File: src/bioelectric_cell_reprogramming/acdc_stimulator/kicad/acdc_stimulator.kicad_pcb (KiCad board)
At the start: 4 copper layers, 139 x 133 mm, 144 parts, among them IC1 AD9833BRM-REEL7, IC2 AD5122BCPZ10-RL7, IC3 LTC3896EFE#PBF, IC4 LTC3637IMSE#PBF, IC5 LTC3637IMSE#PBF, IC6 LTC3637IMSE#PBF, J1 Screw_Terminal_01x02, J2 Conn_ARM_SWD_TagConnect_TC203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, J3 USB_C_Receptacle_USB2.0_14P, J4 S4B-PH-SM4-TB, J5 IPL1-102-01-L-S-K, J6 Screw_Terminal_01x02, J7 IPL1-102-01-L-S-K, J8 6620XX11122_66200211122, J9 6620XX11122_66200211122, Q1 BSZ096N10LS5ATMA1, Q10 BSZ096N10LS5ATMA1, Q11 BSZ096N10LS5ATMA1, Q2 NDT3055L, Q3 BSC520N15NS3G, Q4 BSC520N15NS3G, Q5 IPD320N20N3GATMA1, Q6 BSZ096N10LS5ATMA1, Q7 BSZ096N10LS5ATMA1, Q8 IPB320P10LMATMA1, Q9 IPB320P10LMATMA1, SW1 SW_Push, SW2 SW_SPDT, U1 STM32G473RCTx, U2 AMS1117-3.3, U3 USBLC6-2SC6, U4 LTC6090CFE-PBF, U5 LTC6090CFE-PBF, U7 DRV8873HPWPR, Y1 16Mhz

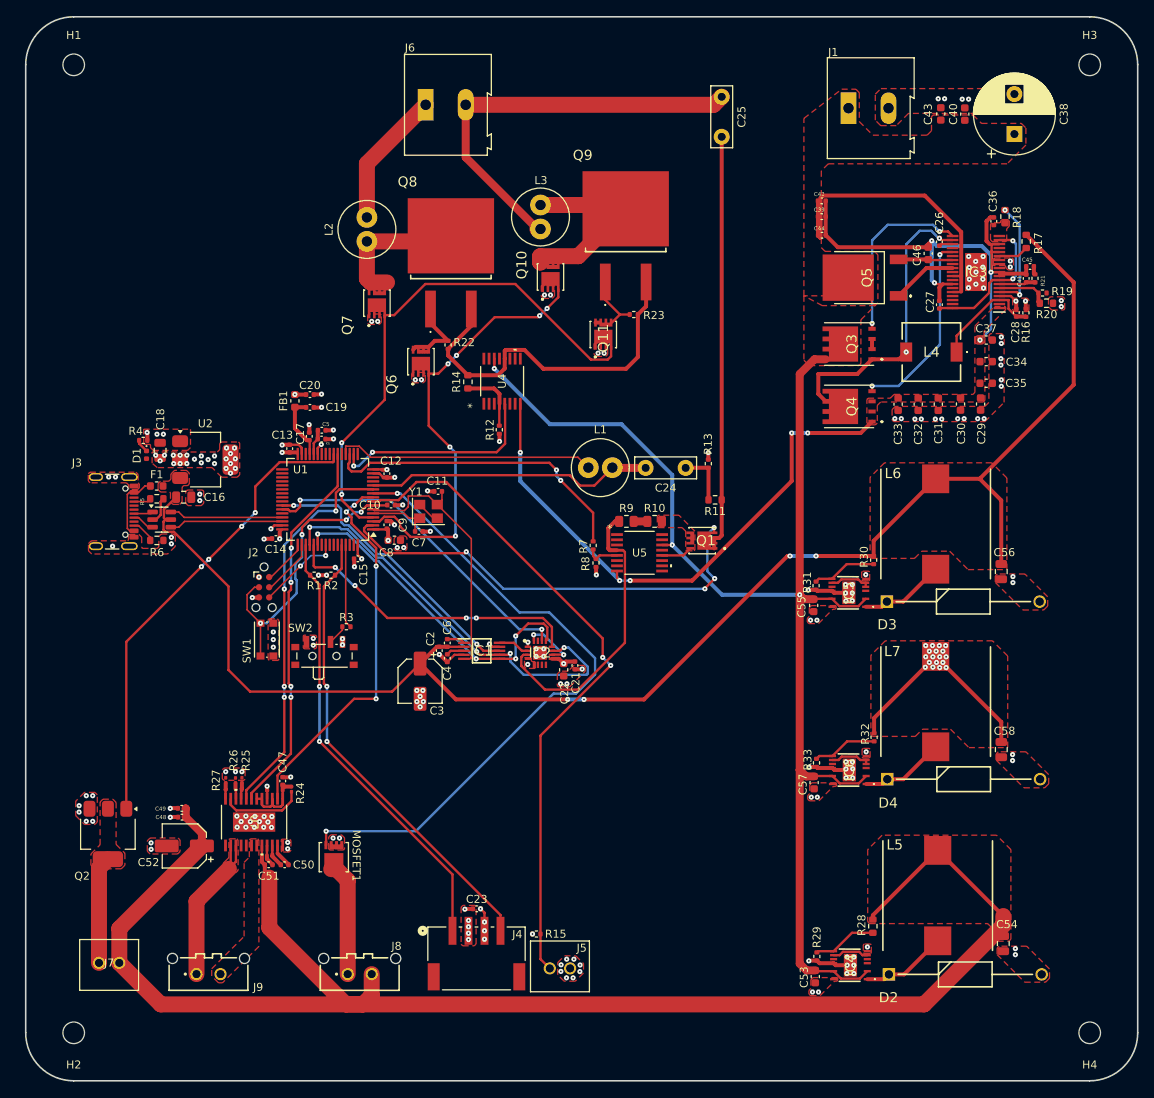
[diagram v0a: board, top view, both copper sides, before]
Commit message: fix: cleared all DRC errors
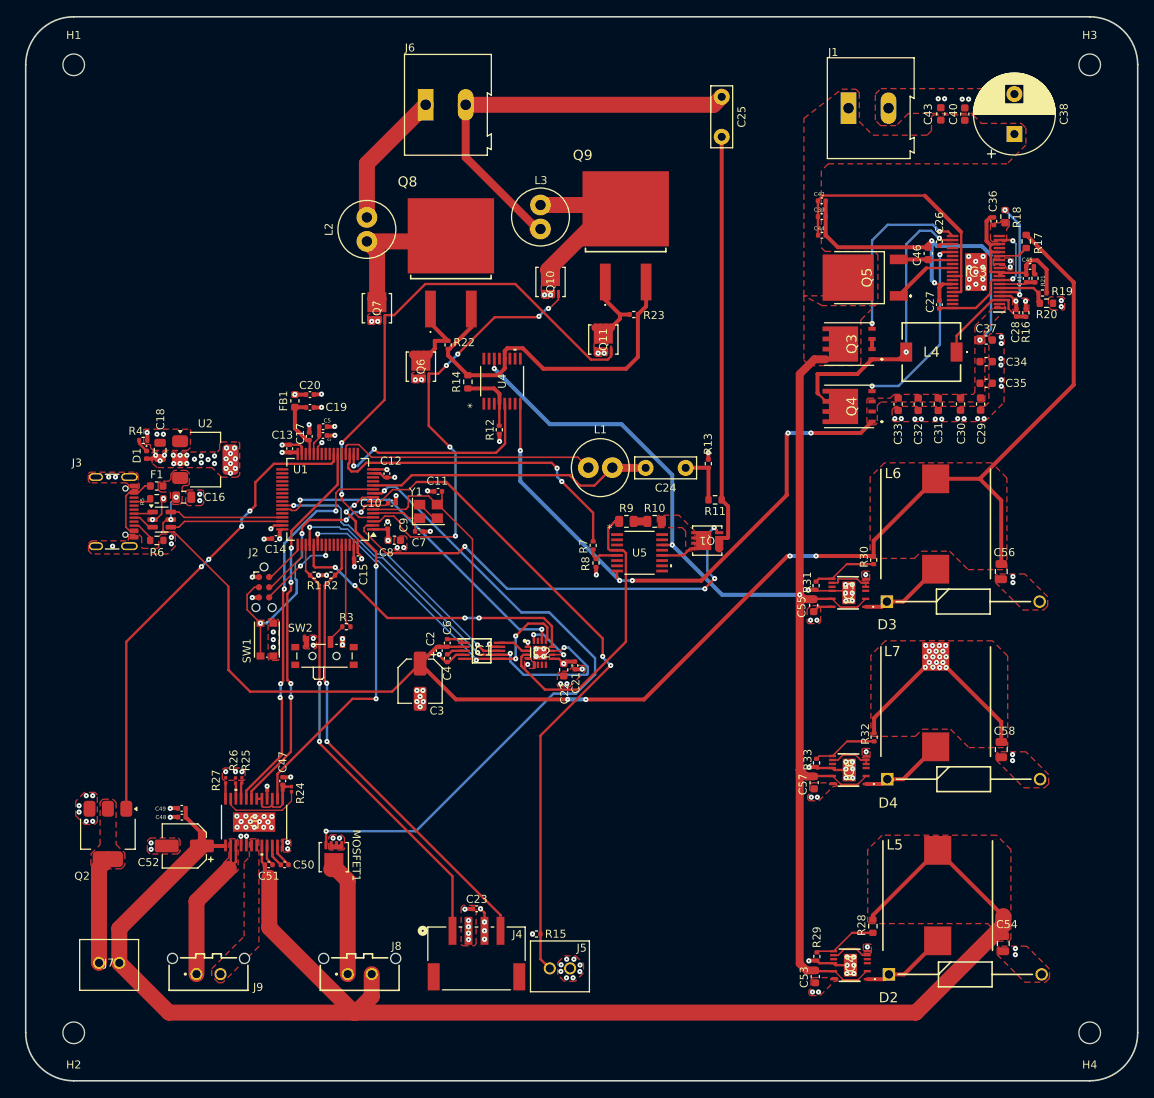
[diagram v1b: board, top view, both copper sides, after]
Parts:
- Q1, Q10, Q11, Q6, Q7: footprint BSZ096N10LS5ATMA1:BSZ060NE2LS -> BSZ070N08LS5ATMA1:TSDSON-8-FL_INF
- moved C1 0.48 mm to (108.2, 73.3)
- moved C5 0.48 mm to (108.2, 72.2)
- moved C10 0.26 mm to (116.8, 81.8)
- moved C9 0.10 mm to (116.2, 84.5)
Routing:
- net -60V: track 138.0 -> 146.6 mm, vias 9 -> 8
- net GND: track 60.2 -> 65.8 mm, vias 188 -> 192
- net +12V: track 199.0 -> 203.7 mm
- net +60V: track 202.6 -> 198.1 mm
- net Net-(Q11-D_1): track 7.93 -> 10.1 mm
- net +3.3V: track 45.8 -> 48.0 mm
- net /V_DC2: track 24.8 -> 23.7 mm
- net Net-(Q6-D_1): track 9.73 -> 10.6 mm
- net /VAC_ON: track 56.9 -> 57.6 mm
- net /INCUBATOR_PELT_OUT: track 81.8 -> 82.5 mm
- net /VREF: track 3.18 -> 3.71 mm
- net +5V: track 193.9 -> 193.5 mm, vias 4 -> 6

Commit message: ci: moved silkscreen items
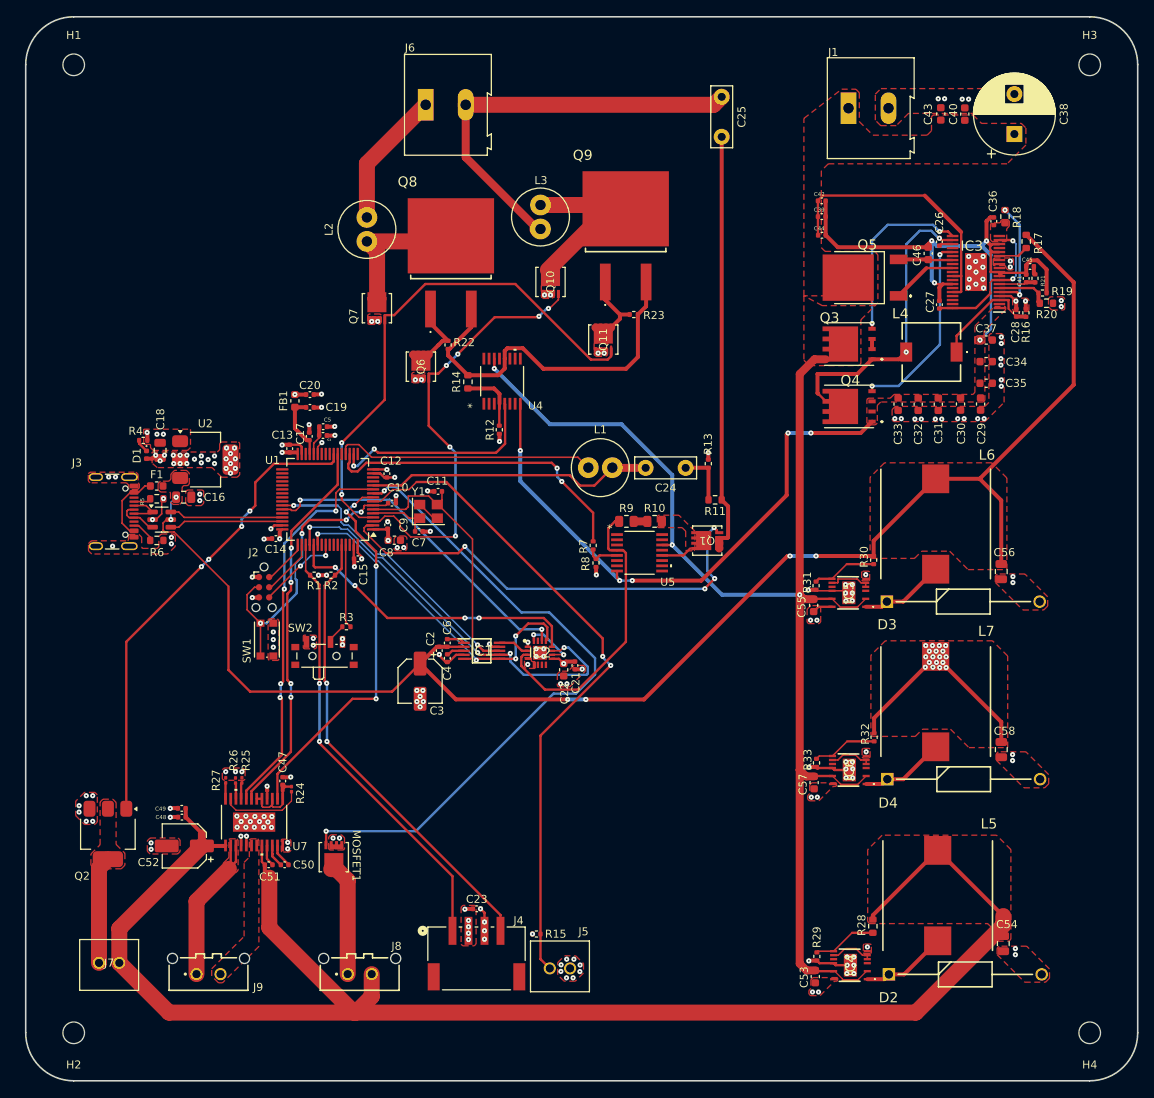
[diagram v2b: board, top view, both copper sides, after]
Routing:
- net Net-(J3-D--PadA7): track 2.41 -> 5.06 mm
- net Net-(J3-D+-PadA6): track 2.82 -> 5.33 mm
- net -60V: track 146.6 -> 147.4 mm, vias 8 -> 9
- net Net-(Q6-D_1): track 10.6 -> 10.0 mm
- net Net-(IC4-SS): track 4.85 -> 5.35 mm
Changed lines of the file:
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@@
 		(tags "Integrated Circuit")
 		(property "Reference" "IC3"
-			(at 0 0 0)
+			(at 0.5375 3.255 0)
 			(layer "F.SilkS")
 			(effects
@@
 		(tags "LQFP QFP")
 		(property "Reference" "U1"
-			(at 3.4 3.725 0)
+			(at 6.9 4.9 0)
 			(layer "F.SilkS")
 			(effects
@@
 		(tags "Inductor")
 		(property "Reference" "L5"
-			(at 6.35 -5.375 0)
+			(at 8.975 6.4 0)
 			(layer "F.SilkS")
 			(effects
@@
 		(tags "capacitor")
 		(property "Reference" "C5"
-			(at 0.515 -0.76 0)
+			(at 0.5425 -0.86 0)
 			(layer "F.SilkS")
 			(effects
@@
 		(tags "Inductor")
 		(property "Reference" "L4"
-			(at 0 0 0)
+			(at 3.8875 4.805 0)
 			(layer "F.SilkS")
 			(effects
@@
 		(tags "SMD SMT crystal")
 		(property "Reference" "Y1"
-			(at -1.6 -2.45 0)
+			(at -1.25 -2.475 0)
 			(layer "F.SilkS")
 			(effects
@@
 		(tags "capacitor")
 		(property "Reference" "C51"
-			(at -0.02 -1.4 0)
+			(at -0.155 -1.5 0)
 			(layer "F.SilkS")
 			(effects
@@
 		(tags "BSZ070N08LS5ATMA1 ")
 		(property "Reference" "Q7"
-			(at 0 0 90)
+			(at -1.025 -2.925 90)
 			(unlocked yes)
 			(layer "F.SilkS")
@@
 		(tags "DRV8873HPWPR ")
 		(property "Reference" "U7"
-			(at 0 0 -90)
+			(at 3.0345 -5.725002 0)
 			(unlocked yes)
 			(layer "F.SilkS")
@@
 		(tags "LTC6090CFE-PBF ")
 		(property "Reference" "U4"
-			(at 0 0 90)
+			(at -3.075 4.175 0)
 			(unlocked yes)
 			(layer "F.SilkS")
@@
 		(tags "LTC6090CFE-PBF ")
 		(property "Reference" "U5"
-			(at 0 0 0)
+			(at 3.5181 3.65 0)
 			(unlocked yes)
 			(layer "F.SilkS")
@@
 		(tags "Inductor")
 		(property "Reference" "L6"
-			(at 6.325 -5.3455 180)
+			(at 8.625 6.4045 180)
 			(layer "F.SilkS")
 			(effects
@@
 		(tags "IPL1-102-01-L-S-K ")
 		(property "Reference" "J5"
-			(at -1.450002 2.549999 0)
+			(at -1.675002 4.599999 0)
 			(unlocked yes)
 			(layer "F.SilkS")
@@
 		(tags "MOSFET (N-Channel)")
 		(property "Reference" "Q5"
-			(at 0 5.55 90)
+			(at 4.105 5.5875 180)
 			(layer "F.SilkS")
 			(effects
@@
 		(tags "MOSFET (N-Channel)")
 		(property "Reference" "Q4"
-			(at 0 0.337 90)
+			(at 3.255 0.15 180)
 			(layer "F.SilkS")
 			(effects
@@
 		(tags "S4B-PH-SM4-TB ")
 		(property "Reference" "J4"
-			(at -5.100001 3.0027 0)
+			(at -5.250001 4.7277 0)
 			(unlocked yes)
 			(layer "F.SilkS")
@@
 		(tags "capacitor")
 		(property "Reference" "C10"
-			(at -2.645 0 0)
+			(at 0.715 -1.936558 0)
 			(layer "F.SilkS")
 			(effects
@@
 		(tags "Inductor")
 		(property "Reference" "L7"
-			(at 6.275 -5.425 0)
+			(at 8.8 6.325 0)
 			(layer "F.SilkS")
 			(effects
@@
 		(tags "MOSFET (N-Channel)")
 		(property "Reference" "Q3"
-			(at 0 0.337 90)
+			(at 3.28 -2.45 180)
 			(layer "F.SilkS")
 			(effects
@@
 	)
 	(via
+		(at 191.1 49.025)
+		(size 0.65)
+		(drill 0.2)
+		(layers "F.Cu" "B.Cu")
+		(net 12)
+	)
+	(via
 		(at 132.82584 75.225)
 		(size 0.65)
@@
 	)
 	(segment
+		(start 190.512161 49.612839)
+		(end 191.1 49.025)
+		(width 0.5)
+		(layer "B.Cu")
+		(net 12)
+	)
+	(segment
 		(start 190.2875 61.405)
 		(end 191.6575 60.035)
@@
 	)
 	(segment
-		(start 191.6575 50.801129)
-		(end 190.512161 49.65579)
+		(start 190.512161 49.65579)
+		(end 191.6575 50.801129)
+		(width 0.5)
+		(layer "B.Cu")
+		(net 12)
+	)
+	(segment
+		(start 190.512161 49.65579)
+		(end 190.512161 49.612839)
 		(width 0.5)
 		(layer "B.Cu")
@@
 	)
 	(segment
+		(start 176.2 138.3)
+		(end 176.2 138.8)
+		(width 0.2)
+		(layer "F.Cu")
+		(net 40)
+	)
+	(segment
 		(start 171.99 138.3)
 		(end 172.575 138.3)
@@
 	)
 	(segment
-		(start 83.525 80.887501)
-		(end 83.525 84.775)
+		(start 84.08009 80.45)
+		(end 83.05 81.48009)
 		(width 0.2)
 		(layer "F.Cu")
@@
 	)
 	(segment
-		(start 83.962501 80.45)
-		(end 83.525 80.887501)
+		(start 83.05 84.3)
+		(end 84 85.25)
 		(width 0.2)
 		(layer "F.Cu")
@@
 	(segment
 		(start 84.5375 80.45)
-		(end 83.962501 80.45)
+		(end 84.08009 80.45)
 		(width 0.2)
 		(layer "F.Cu")
@@
 	)
 	(segment
-		(start 85.1 80.45)
-		(end 85.9 79.65)
+		(start 83.05 81.48009)
+		(end 83.05 84.3)
 		(width 0.2)
 		(layer "F.Cu")
@@
 	)
 	(segment
-		(start 83.525 84.775)
-		(end 84 85.25)
+		(start 85.1 80.45)
+		(end 85.9 79.65)
 		(width 0.2)
 		(layer "F.Cu")
@@
 	)
 	(segment
+		(start 86.0625 82.1)
+		(end 84.5375 82.1)
+		(width 0.2)
+		(layer "F.Cu")
+		(net 125)
+	)
+	(segment
 		(start 84.5375 83.1)
 		(end 86.6625 83.1)
@@
 	)
 	(segment
+		(start 86.8625 82.9)
+		(end 86.0625 82.1)
+		(width 0.2)
+		(layer "F.Cu")
+		(net 125)
+	)
+	(segment
 		(start 86.6625 83.1)
 		(end 86.8625 82.9)
@@
 	)
 	(segment
+		(start 83.93009 83.6)
+		(end 83.65 83.31991)
+		(width 0.2)
+		(layer "F.Cu")
+		(net 126)
+	)
+	(segment
+		(start 83.65 83.31991)
+		(end 83.65 82.78009)
+		(width 0.2)
+		(layer "F.Cu")
+		(net 126)
+	)
+	(segment
 		(start 84.5375 83.6)
 		(end 85.25 83.6)
@@
 	)
 	(segment
+		(start 84.5375 83.6)
+		(end 83.93009 83.6)
+		(width 0.2)
+		(layer "F.Cu")
+		(net 126)
+	)
+	(segment
+		(start 83.65 82.78009)
+		(end 83.83009 82.6)
+		(width 0.2)
+		(layer "F.Cu")
+		(net 126)
+	)
+	(segment
+		(start 83.83009 82.6)
+		(end 84.5375 82.6)
+		(width 0.2)
+		(layer "F.Cu")
+		(net 126)
+	)
+	(segment
 		(start 84.5375 81.6)
 		(end 86.2125 81.6)
@@
 	)
 	(segment
-		(start 122.135 61.505)
-		(end 123.8 61.505)
-		(width 0.5)
-		(layer "F.Cu")
-		(net 132)
-	)
-	(segment
-		(start 122.135 61.505)
-		(end 122.135 62.492)
+		(start 122.6 62.027)
+		(end 121.3906 63.2364)
 		(width 0.5)
 		(layer "F.Cu")
@@
 	)
 	(segment
+		(start 122.6 62.025)
+		(end 122.6 62.027)
+		(width 0.5)
+		(layer "F.Cu")
+		(net 132)
+	)
+	(segment
+		(start 123.8 61.505)
+		(end 123.12 61.505)
+		(width 0.5)
+		(layer "F.Cu")
+		(net 132)
+	)
+	(segment
 		(start 121.6 59.305)
 		(end 123.8 61.505)
@@
 	)
 	(segment
-		(start 122.135 62.492)
-		(end 121.3906 63.2364)
+		(start 123.12 61.505)
+		(end 122.6 62.025)
 		(width 0.5)
 		(layer "F.Cu")

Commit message: fix: updated old footprints
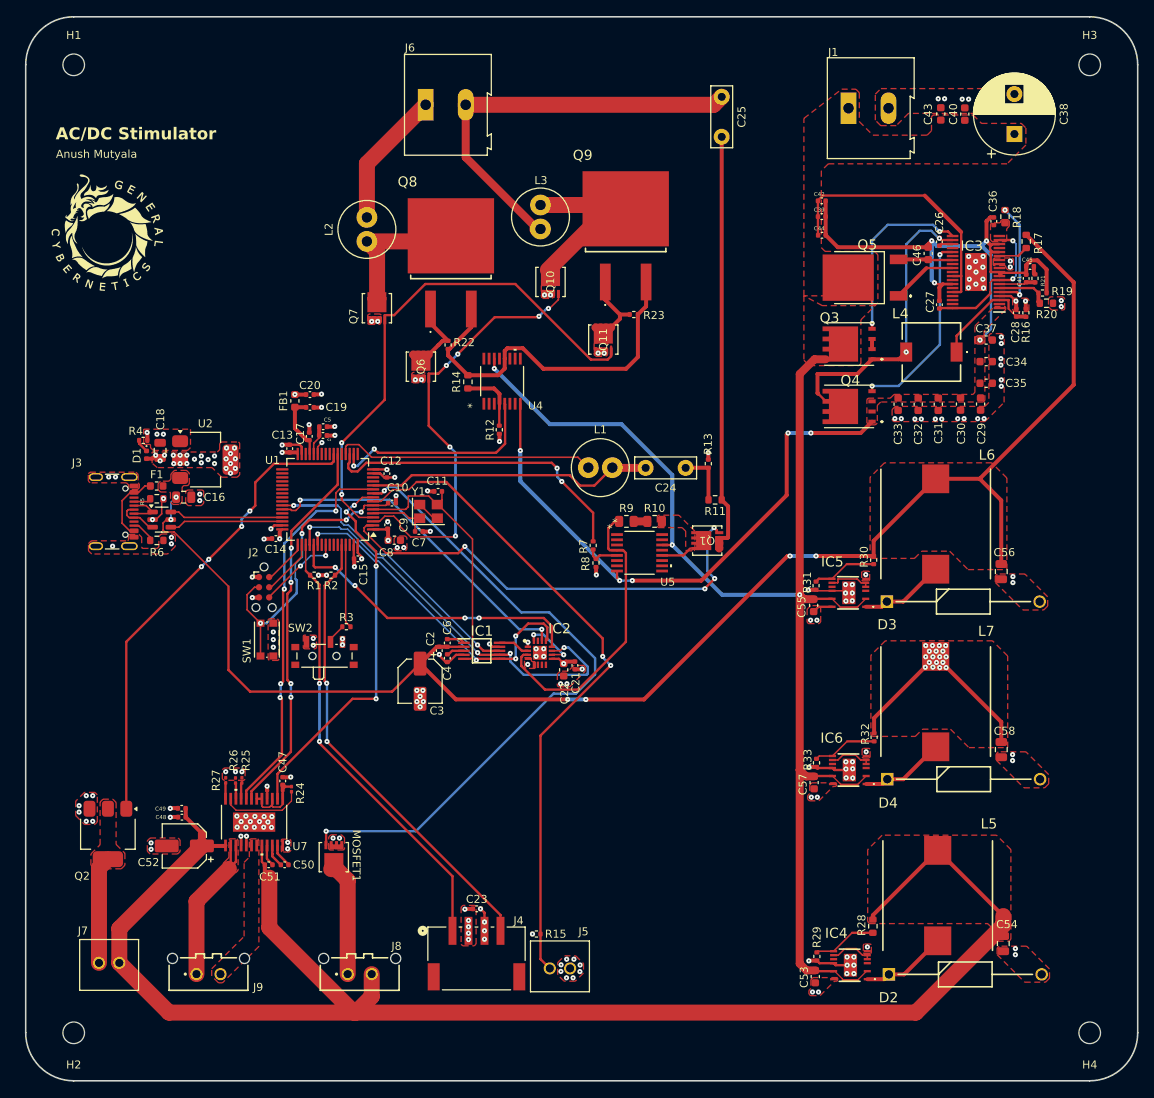
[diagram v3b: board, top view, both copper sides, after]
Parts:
- added G***: LOGO, LOGO, F.Cu at (81.2, 48.0)
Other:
- board text added: "AC/DC Stimulator"
- board text added: "Anush Mutyala"

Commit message: all drc errors cleared
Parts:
- Q1, Q10, Q11, Q6, Q7: footprint BSZ070N08LS5ATMA1:TSDSON-8-FL_INF -> BSZ096N10LS5ATMA1:BSZ060NE2LS
- moved J3 7.23 mm to (73.6, 82.8)
- moved R5 7.23 mm to (80.2, 81.2)
- moved R6 7.23 mm to (80.2, 86.5)
- moved U2 7.23 mm to (86.2, 76.3)
- moved C16 7.22 mm to (83.5, 81.0)
- moved C18 7.22 mm to (80.6, 75.2)
- moved D1 7.22 mm to (78.9, 75.8)
- moved F1 7.22 mm to (80.2, 79.7)
- moved R4 7.22 mm to (78.5, 74.0)
- moved U3 7.22 mm to (80.8, 83.8)
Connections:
- Q4 pad 5: Net-(Q4-D_1) -> /DCDC_inverter/SW
- Q4 pad 7: Net-(Q4-D_1) -> /DCDC_inverter/SW
- Q4 pad 8: Net-(Q4-D_1) -> /DCDC_inverter/SW
- Q4 pad 9: Net-(Q4-D_1) -> /DCDC_inverter/SW
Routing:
- net +5V: track 193.5 -> 200.7 mm
- net /USB_D-: track 14.2 -> 21.4 mm
- net /USB_D+: track 14.2 -> 21.5 mm
- net /VAC_ON: track 57.6 -> 53.5 mm
- net /DCDC_inverter/SW: track 36.6 -> 40.4 mm
- net /H_Bridge_IN2: track 65.4 -> 63.3 mm
- net /H_Bridge_IN1: track 54.4 -> 56.4 mm
- net /V_AC: track 52.6 -> 53.4 mm
- net Net-(Q11-D_1): track 10.1 -> 9.48 mm
